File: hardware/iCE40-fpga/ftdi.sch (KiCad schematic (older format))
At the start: 19 parts, among them U7 93C46B, U8 FT2232H

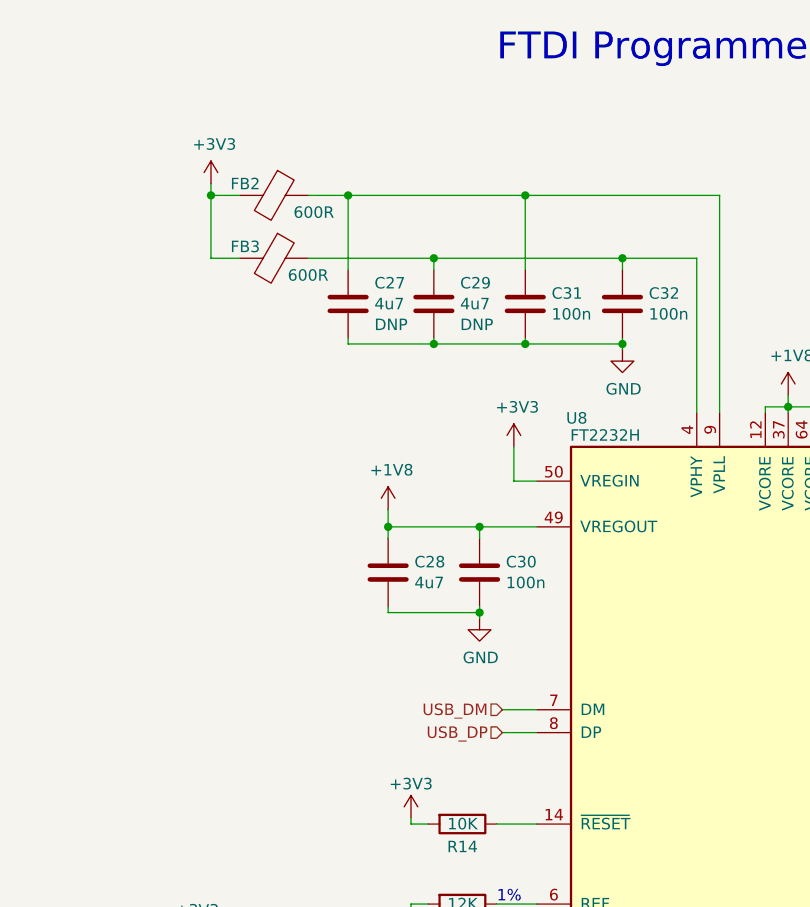
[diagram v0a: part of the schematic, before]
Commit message: fixed footprints + added extra feather headers
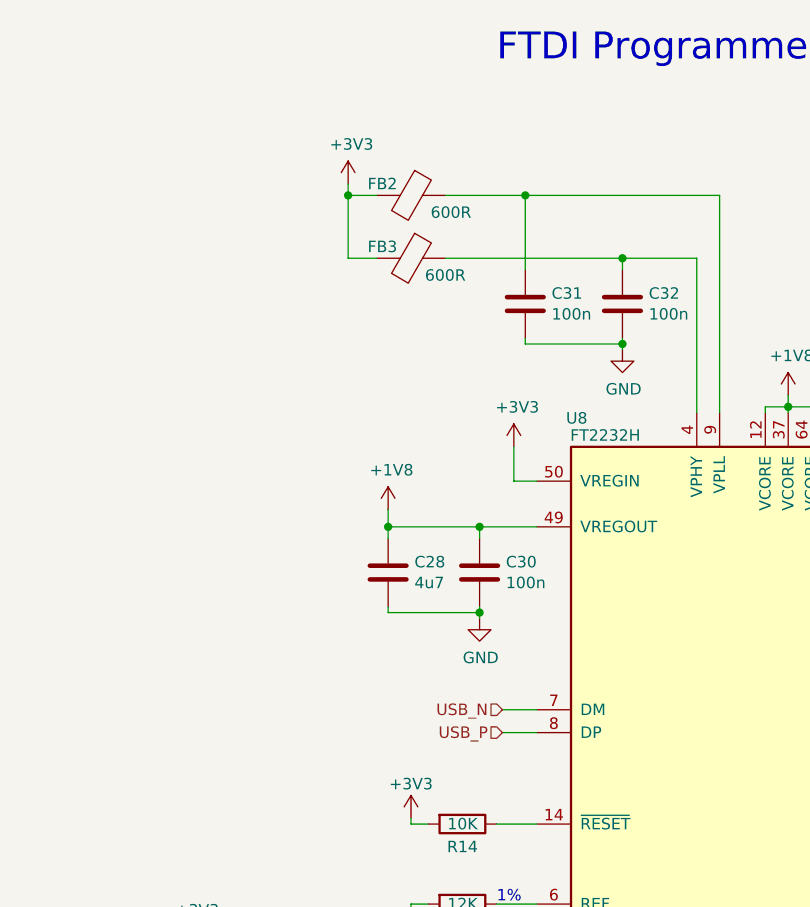
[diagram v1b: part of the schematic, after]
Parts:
- removed C27, C29: 4u7, Capacitor_SMD:C_0603_1608Metric, symbol Device:C
- U8: footprint Package_DFN_QFN:QFN-64-1EP_9x9mm_P0.5mm_EP4.7x4.7mm_ThermalVias -> josh-footprints:QFN-64-1EP_9x9mm_P0.5mm_EP4.7x4.7mm_ThermalVias
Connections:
- net USB_DM renamed USB_N
- net USB_DP renamed USB_P
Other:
- moved on the sheet: FB2, FB3
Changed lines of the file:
@@
 F 0 "U8" H 4200 6850 50  0000 C CNN
 F 1 "FT2232H" H 4325 6775 50  0000 C CNN
-F 2 "Package_DFN_QFN:QFN-64-1EP_9x9mm_P0.5mm_EP4.7x4.7mm_ThermalVias" H 5225 4675 50  0001 C CNN
+F 2 "josh-footprints:QFN-64-1EP_9x9mm_P0.5mm_EP4.7x4.7mm_ThermalVias" H 5225 4675 50  0001 C CNN
 F 3 "http://www.ftdichip.com/Products/ICs/FT2232H.html" H 5225 4675 50  0001 C CNN
 	1    5225 4675
@@
 $EndComp
 Text HLabel 3875 3775 0    50   Input ~ 0
-USB_DM
+USB_N
 Text HLabel 3875 3875 0    50   Input ~ 0
-USB_DP
+USB_P
 Wire Wire Line
 	5525 2425 5425 2425
@@
 Wire Wire Line
 	5125 2450 5225 2450
-Connection ~ 2600 1525
+Connection ~ 3200 1525
 Wire Wire Line
 	4400 1800 4725 1800
@@
 Wire Wire Line
 	4400 1850 4400 1800
-Wire Wire Line
-	3975 1525 3200 1525
 Connection ~ 3975 1525
 Wire Wire Line
 	3975 1850 3975 1525
 Wire Wire Line
-	3575 1800 4400 1800
-Connection ~ 3575 1800
-Wire Wire Line
-	3575 1850 3575 1800
-Wire Wire Line
-	3200 1525 3025 1525
-Connection ~ 3200 1525
-Wire Wire Line
-	3200 1850 3200 1525
-Wire Wire Line
 	4825 1525 3975 1525
 Wire Wire Line
@@
 Wire Wire Line
 	4725 1800 4725 2475
-Wire Wire Line
-	3025 1800 3575 1800
 $Comp
 L power:GND #PWR?
@@
 $EndComp
 Wire Wire Line
-	3975 2175 3575 2175
-Connection ~ 3975 2175
-Wire Wire Line
 	3975 2150 3975 2175
-Wire Wire Line
-	3575 2175 3200 2175
-Connection ~ 3575 2175
-Wire Wire Line
-	3575 2150 3575 2175
 Wire Wire Line
 	4400 2175 4400 2200
 Connection ~ 4400 2175
-Wire Wire Line
-	3200 2175 3200 2150
 Wire Wire Line
 	4400 2175 3975 2175
@@
 	1    0    0    -1
 $EndComp
-$Comp
-L Device:C C?
-U 1 1 5EDD47F7
-P 3575 2000
-AR Path="/5EDD47F7" Ref="C?"  Part="1"
-AR Path="/5ED7AB6B/5EDD47F7" Ref="C29"  Part="1"
-F 0 "C29" H 3690 2091 50  0000 L CNN
-F 1 "4u7" H 3690 2000 50  0000 L CNN
-F 2 "Capacitor_SMD:C_0603_1608Metric" H 3613 1850 50  0001 C CNN
-F 3 "~" H 3575 2000 50  0001 C CNN
-F 4 "DNP" H 3690 1909 50  0000 L CNN "DNP"
-	1    3575 2000
-	1    0    0    -1
-$EndComp
-$Comp
-L Device:C C?
-U 1 1 5EDD47F0
-P 3200 2000
-AR Path="/5EDD47F0" Ref="C?"  Part="1"
-AR Path="/5ED7AB6B/5EDD47F0" Ref="C27"  Part="1"
-F 0 "C27" H 3315 2091 50  0000 L CNN
-F 1 "4u7" H 3315 2000 50  0000 L CNN
-F 2 "Capacitor_SMD:C_0603_1608Metric" H 3238 1850 50  0001 C CNN
-F 3 "~" H 3200 2000 50  0001 C CNN
-F 4 "DNP" H 3315 1909 50  0000 L CNN "DNP"
-	1    3200 2000
-	1    0    0    -1
-$EndComp
-Wire Wire Line
-	2600 1800 2600 1525
-Wire Wire Line
-	2725 1800 2600 1800
+Wire Wire Line
+	3200 1800 3200 1525
+Wire Wire Line
+	3325 1800 3200 1800
 $Comp
 L josh-symbols:Ferrite_Bead_PWR FB?
 U 1 1 5EDD47E7
-P 2875 1800
+P 3475 1800
 AR Path="/5EDD47E7" Ref="FB?"  Part="1"
 AR Path="/5ED7AB6B/5EDD47E7" Ref="FB3"  Part="1"
-F 0 "FB3" V 2825 1675 50  0000 C CNN
-F 1 "600R " V 2950 1950 50  0000 C CNN
-F 2 "josh-footprints:BEADC1608X95N" V 2805 1800 50  0001 C CNN
-F 3 "~" H 2875 1800 50  0001 C CNN
-	1    2875 1800
+F 0 "FB3" V 3425 1675 50  0000 C CNN
+F 1 "600R " V 3550 1950 50  0000 C CNN
+F 2 "josh-footprints:BEADC1608X95N" V 3405 1800 50  0001 C CNN
+F 3 "~" H 3475 1800 50  0001 C CNN
+	1    3475 1800
 	0    1    1    0
 $EndComp
@@
 L josh-symbols:Ferrite_Bead_PWR FB?
 U 1 1 5EDD47E1
-P 2875 1525
+P 3475 1525
 AR Path="/5EDD47E1" Ref="FB?"  Part="1"
 AR Path="/5ED7AB6B/5EDD47E1" Ref="FB2"  Part="1"
-F 0 "FB2" V 2825 1400 50  0000 C CNN
-F 1 "600R " V 2950 1700 50  0000 C CNN
-F 2 "josh-footprints:BEADC1608X95N" V 2805 1525 50  0001 C CNN
-F 3 "~" H 2875 1525 50  0001 C CNN
-	1    2875 1525
+F 0 "FB2" V 3425 1400 50  0000 C CNN
+F 1 "600R " V 3550 1700 50  0000 C CNN
+F 2 "josh-footprints:BEADC1608X95N" V 3405 1525 50  0001 C CNN
+F 3 "~" H 3475 1525 50  0001 C CNN
+	1    3475 1525
 	0    1    1    0
 $EndComp
 Wire Wire Line
-	2600 1525 2725 1525
-Wire Wire Line
-	2600 1475 2600 1525
+	3200 1525 3325 1525
+Wire Wire Line
+	3200 1475 3200 1525
 $Comp
 L power:+3V3 #PWR?
 U 1 1 5EDD47D9
-P 2600 1475
+P 3200 1475
 AR Path="/5EDD47D9" Ref="#PWR?"  Part="1"
 AR Path="/5ED7AB6B/5EDD47D9" Ref="#PWR059"  Part="1"
-F 0 "#PWR059" H 2600 1325 50  0001 C CNN
-F 1 "+3V3" H 2615 1648 50  0000 C CNN
-F 2 "" H 2600 1475 50  0001 C CNN
-F 3 "" H 2600 1475 50  0001 C CNN
-	1    2600 1475
+F 0 "#PWR059" H 3200 1325 50  0001 C CNN
+F 1 "+3V3" H 3215 1648 50  0000 C CNN
+F 2 "" H 3200 1475 50  0001 C CNN
+F 3 "" H 3200 1475 50  0001 C CNN
+	1    3200 1475
 	1    0    0    -1
 $EndComp
@@
 	1    0    0    -1
 $EndComp
+Wire Wire Line
+	3625 1800 4400 1800
+Wire Wire Line
+	3625 1525 3975 1525
 $EndSCHEMATC

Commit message: all nets routed
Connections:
- net FT_EECLK: now also RN2.3 (R3.1); no longer RN2.2 (R2.1)
- net FT_EECS: now also RN2.2 (R2.1); no longer RN2.1 (R1.1)
- net FT_EEDATA: now also RN2.4 (R4.1); no longer RN2.3 (R3.1)
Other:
- moved on the sheet: RN2
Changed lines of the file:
@@
 Text Label 2925 5575 0    50   ~ 0
 FT_EEDATA
-$Comp
-L Device:R_Pack04 RN?
-U 1 1 5EDD474C
-P 2725 5125
-AR Path="/5EDD474C" Ref="RN?"  Part="1"
-AR Path="/5ED7AB6B/5EDD474C" Ref="RN2"  Part="1"
-F 0 "RN2" H 2913 5171 50  0000 L CNN
-F 1 "10K" H 2913 5080 50  0000 L CNN
-F 2 "Resistor_SMD:R_Array_Convex_4x0402" V 3000 5125 50  0001 C CNN
-F 3 "~" H 2725 5125 50  0001 C CNN
-	1    2725 5125
-	1    0    0    -1
-$EndComp
-Wire Wire Line
-	2525 5325 2525 5375
 Connection ~ 2525 5375
 Wire Wire Line
 	2525 5375 4025 5375
-Wire Wire Line
-	2625 5325 2625 5475
 Connection ~ 2625 5475
 Wire Wire Line
 	2625 5475 4025 5475
-Wire Wire Line
-	2725 5325 2725 5575
 Connection ~ 2725 5575
-NoConn ~ 2825 5325
-Wire Wire Line
-	2725 4925 2725 4875
-Wire Wire Line
-	2725 4875 2625 4875
-Wire Wire Line
-	2525 4875 2525 4925
-Wire Wire Line
-	2625 4875 2625 4925
-Connection ~ 2625 4875
-Wire Wire Line
-	2625 4875 2525 4875
-Wire Wire Line
-	2525 4875 2525 4825
-Connection ~ 2525 4875
-$Comp
-L power:+3V3 #PWR?
-U 1 1 5EDD4764
-P 2525 4825
-AR Path="/5EDD4764" Ref="#PWR?"  Part="1"
-AR Path="/5ED7AB6B/5EDD4764" Ref="#PWR058"  Part="1"
-F 0 "#PWR058" H 2525 4675 50  0001 C CNN
-F 1 "+3V3" H 2540 4998 50  0000 C CNN
-F 2 "" H 2525 4825 50  0001 C CNN
-F 3 "" H 2525 4825 50  0001 C CNN
-	1    2525 4825
-	1    0    0    -1
-$EndComp
 $Comp
 L Device:R R?
@@
 NoConn ~ 6425 6375
 NoConn ~ 6425 6475
-Wire Wire Line
-	2725 4875 2825 4875
-Wire Wire Line
-	2825 4875 2825 4925
-Connection ~ 2725 4875
 $Comp
 L josh-symbols:93C46B U7
@@
 Wire Wire Line
 	3625 1525 3975 1525
+Wire Wire Line
+	2725 5250 2725 5575
+Wire Wire Line
+	2625 5250 2625 5475
+Wire Wire Line
+	2525 5250 2525 5375
+Connection ~ 2625 4800
+Wire Wire Line
+	2725 4800 2725 4850
+Wire Wire Line
+	2625 4800 2725 4800
+$Comp
+L power:+3V3 #PWR?
+U 1 1 5EDD4764
+P 2425 4750
+AR Path="/5EDD4764" Ref="#PWR?"  Part="1"
+AR Path="/5ED7AB6B/5EDD4764" Ref="#PWR058"  Part="1"
+F 0 "#PWR058" H 2425 4600 50  0001 C CNN
+F 1 "+3V3" H 2440 4923 50  0000 C CNN
+F 2 "" H 2425 4750 50  0001 C CNN
+F 3 "" H 2425 4750 50  0001 C CNN
+	1    2425 4750
+	1    0    0    -1
+$EndComp
+Connection ~ 2425 4800
+Wire Wire Line
+	2425 4800 2425 4750
+Wire Wire Line
+	2525 4800 2425 4800
+Connection ~ 2525 4800
+Wire Wire Line
+	2525 4800 2525 4850
+Wire Wire Line
+	2425 4800 2425 4850
+Wire Wire Line
+	2625 4800 2525 4800
+Wire Wire Line
+	2625 4850 2625 4800
+NoConn ~ 2425 5250
+$Comp
+L Device:R_Pack04 RN?
+U 1 1 5EDD474C
+P 2625 5050
+AR Path="/5EDD474C" Ref="RN?"  Part="1"
+AR Path="/5ED7AB6B/5EDD474C" Ref="RN2"  Part="1"
+F 0 "RN2" H 2813 5096 50  0000 L CNN
+F 1 "10K" H 2813 5005 50  0000 L CNN
+F 2 "Resistor_SMD:R_Array_Convex_4x0402" V 2900 5050 50  0001 C CNN
+F 3 "~" H 2625 5050 50  0001 C CNN
+	1    2625 5050
+	1    0    0    -1
+$EndComp
 $EndSCHEMATC

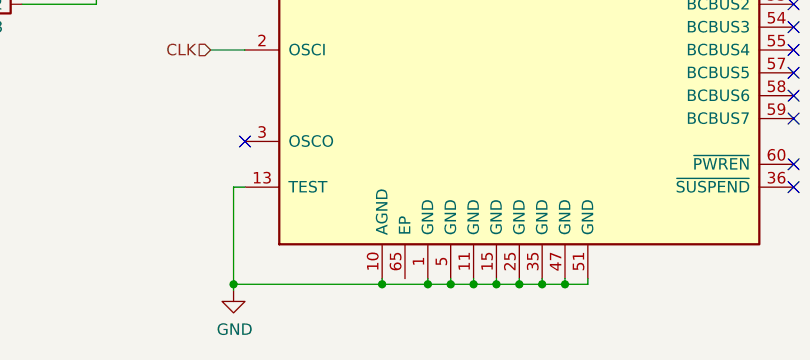
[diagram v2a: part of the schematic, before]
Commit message: added tx, rx leds, 7 segment and pmod wings
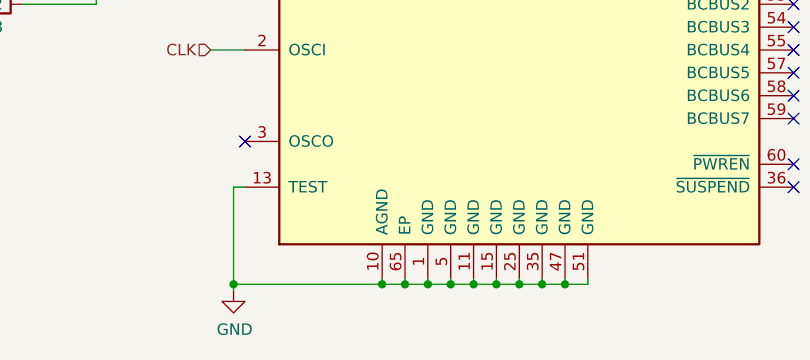
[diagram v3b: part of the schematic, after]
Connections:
- net GND: now also U8.65 (EP)
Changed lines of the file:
@@
 	5025 6900 5125 6900
 Wire Wire Line
-	4625 6900 4825 6900
+	4625 6900 4725 6900
 Wire Wire Line
 	3975 6900 4625 6900
@@
 	1    0    0    -1
 $EndComp
+Wire Wire Line
+	4725 6875 4725 6900
+Connection ~ 4725 6900
+Wire Wire Line
+	4725 6900 4825 6900
 $EndSCHEMATC
